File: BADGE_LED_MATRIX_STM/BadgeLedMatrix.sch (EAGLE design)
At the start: 106 parts, among them CN2 MICRO-USB-5P-340015001, IC1 STM32F0P, IC2 REG1117, Q1 12MHz, Q2 8MHz, U1 USBLC6SOT-23

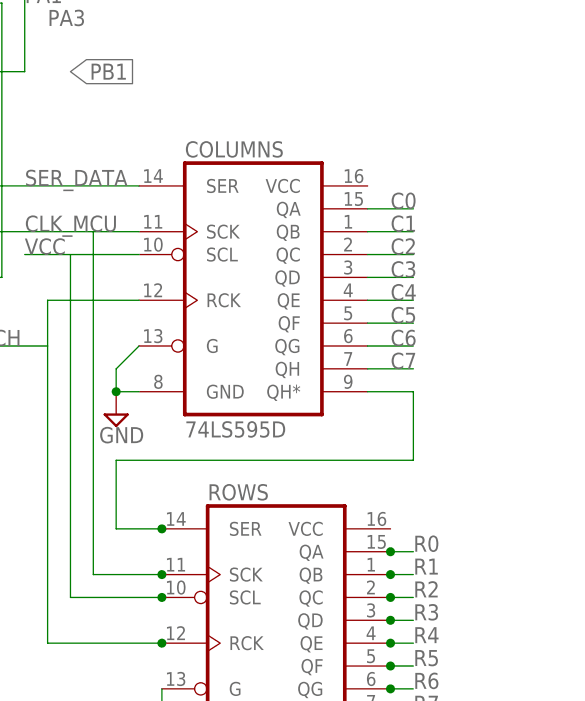
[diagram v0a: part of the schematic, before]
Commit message: Fix for connection of VCC from shift registers
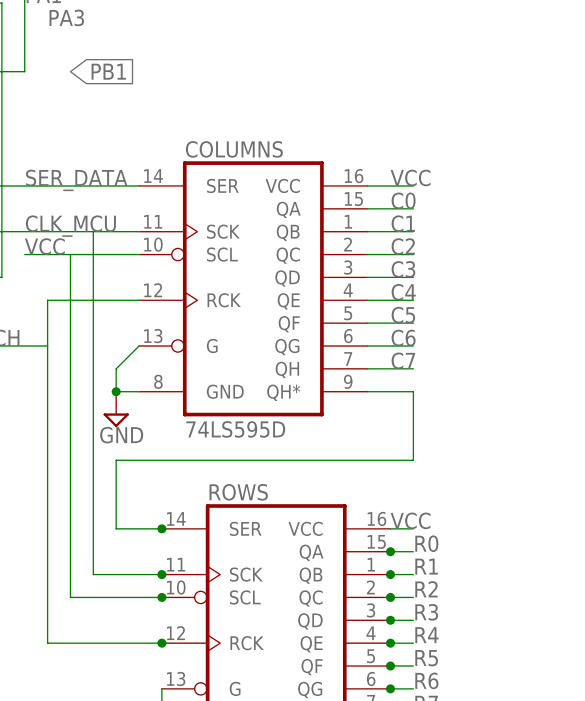
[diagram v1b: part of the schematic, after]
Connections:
- net VCC: now also COLUMNS.VCC, ROWS.VCC
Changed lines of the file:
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@@
 <label x="401.32" y="314.96" size="1.778" layer="95"/>
+</segment>
+<segment>
+<pinref part="COLUMNS" gate="A" pin="VCC"/>
+<wire x1="467.36" y1="289.56" x2="472.44" y2="289.56" width="0.1524" layer="91"/>
+<label x="469.9" y="289.56" size="1.778" layer="95"/>
+</segment>
+<segment>
+<pinref part="ROWS" gate="A" pin="VCC"/>
+<wire x1="469.9" y1="251.46" x2="472.44" y2="251.46" width="0.1524" layer="91"/>
+<label x="469.9" y="251.46" size="1.778" layer="95"/>
 </segment>
 </net>

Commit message: Small touch ups
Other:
- note added: "2"
- note added: "BSidesPR 2016 Led Matrix Badge"
- note added: "BSidesPR2016SCH"
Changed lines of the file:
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@@
 <wire x1="299.72" y1="243.84" x2="345.44" y2="243.84" width="0.1524" layer="94"/>
 <wire x1="345.44" y1="243.84" x2="345.44" y2="210.82" width="0.1524" layer="94"/>
+<text x="398.78" y="139.7" size="2.54" layer="94">BSidesPR 2016 Led Matrix Badge</text>
+<text x="411.48" y="129.54" size="2.54" layer="94">BSidesPR2016SCH</text>
+<text x="477.52" y="129.54" size="2.54" layer="94">2</text>
 </plain>
 <instances>
@@
 <instance part="PROTO1" gate="A" x="480.06" y="320.04"/>
 <instance part="FRAME1" gate="G$1" x="210.82" y="121.92"/>
-<instance part="FRAME1" gate="G$2" x="383.54" y="121.92"/>
+<instance part="FRAME1" gate="G$2" x="383.54" y="121.92" smashed="yes">
+<attribute name="LAST_DATE_TIME" x="396.24" y="123.19" size="2.54" layer="94"/>
+<attribute name="SHEET" x="469.9" y="123.19" size="2.54" layer="94"/>
+</instance>
 </instances>
 <busses>

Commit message: Added EPROM and wired up buttons
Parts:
- removed BTN1, BTN2, BTN3, BTN4: SWITCH-MOMENTARY-2SMD-REDUNDANT, SparkFun-Electromechanical:SWITCH-MOMENTARY-2SMD-REDUNDANT
- removed JP3: (no value), pinhead:PINHD-2X4
- removed JP4: (no value), pinhead:PINHD-2X2
- added DOWN, LEFT, RIGHT, UP: SWITCH-MOMENTARY-2SMD-REDUNDANT, SparkFun-Electromechanical:SWITCH-MOMENTARY-2SMD-REDUNDANT
- added U$6: AT93C66A, digital-ic:AT93C66A
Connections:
- removed net BTN1: BTN1.1, JP4.2
- removed net BTN2: BTN2.1, JP4.4
- removed net BTN3: BTN3.1, JP4.3
- removed net BTN4: BTN4.1, JP4.1
- net CLK_MCU: now also U$6.SK
- net GND: now also DOWN.2, LEFT.2, RIGHT.2, U$6.GND, UP.2; no longer BTN1.2, BTN2.2, BTN3.2, BTN4.2
- net PA0: now also UP.1; no longer JP3.3
- net PA1: now also LEFT.1; no longer JP3.6
- net PA2: now also RIGHT.1; no longer JP3.5
- net PA3: now also U$6.CS; no longer JP3.8
- net PA6: now also U$6.DO; no longer JP3.7
- net PB1: now also DOWN.1; no longer JP3.4
- net SER_DATA: now also U$6.DI
- net VCC: now also U$6.ORG, U$6.VCC; no longer JP3.1
- net VDDA: no longer JP3.2
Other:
- note added: "3"
- note added: "PROGRAM DEBUG ST-LINK"
- note added: "TOP BUTTONS"
- note removed: "2"
- moved on the sheet: JP2, PROTO, PROTO1, ST-LINK

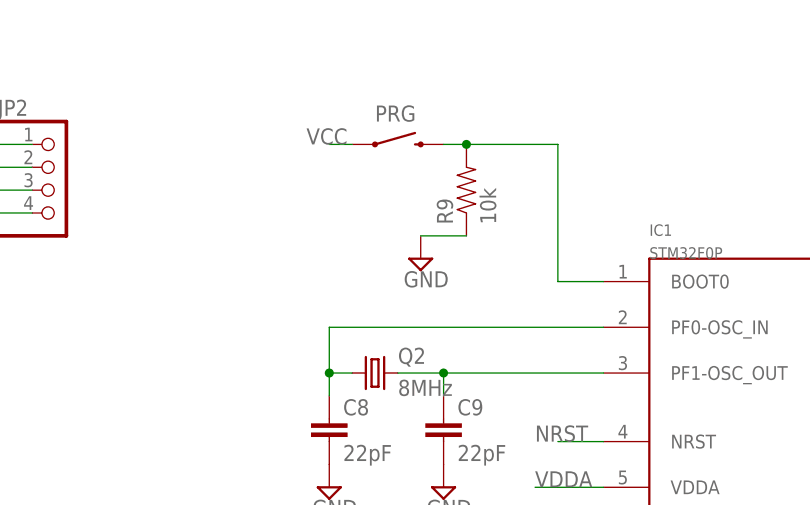
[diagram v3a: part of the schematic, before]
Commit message: Prototype 2, Ordered. Added EPROM, Slide Switch for PROG
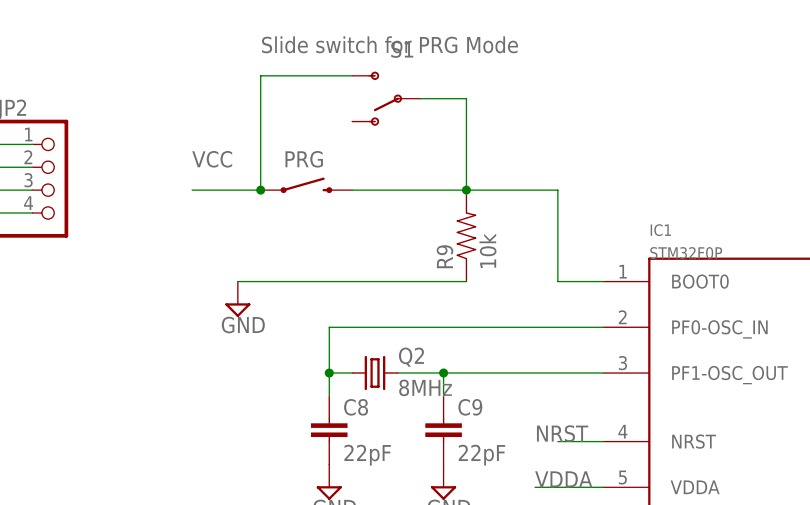
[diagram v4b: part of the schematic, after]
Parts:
- added S1: (no value), SparkFun-Electromechanical:SWITCH-SPDT-SMD-A
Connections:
- net N$4: now also S1.P
- net VCC: now also S1.S
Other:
- note added: "Slide switch for PRG Mode"
- moved on the sheet: PRG, R9
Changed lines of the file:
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@@
 <layer number="91" name="Nets" color="2" fill="1" visible="yes" active="yes"/>
 <layer number="92" name="Busses" color="1" fill="1" visible="yes" active="yes"/>
-<layer number="93" name="Pins" color="2" fill="1" visible="no" active="yes"/>
+<layer number="93" name="Pins" color="2" fill="1" visible="yes" active="yes"/>
 <layer number="94" name="Symbols" color="4" fill="1" visible="yes" active="yes"/>
 <layer number="95" name="Names" color="7" fill="1" visible="yes" active="yes"/>
@@
 <part name="U$6" library="digital-ic" deviceset="AT93C66A" device=""/>
 <part name="SUPPLY9" library="supply2" deviceset="GND" device=""/>
+<part name="S1" library="SparkFun-Electromechanical" deviceset="SWITCH-SPDT" device="-SMD-A"/>
 </parts>
 <sheets>
@@
 <text x="220.98" y="325.12" size="2.54" layer="95">TOP BUTTONS</text>
 <wire x1="248.92" y1="334.01" x2="248.92" y2="284.48" width="0.1524" layer="94"/>
+<text x="330.2" y="330.2" size="1.778" layer="96">Slide switch for PRG Mode</text>
 </plain>
 <instances>
@@
 </instance>
 <instance part="SUPPLY4" gate="GND" x="241.3" y="299.72"/>
-<instance part="R9" gate="G$1" x="353.06" y="314.96" rot="R90"/>
-<instance part="SUPPLY12" gate="GND" x="347.98" y="307.34"/>
-<instance part="PRG" gate="G$1" x="345.44" y="320.04" smashed="yes">
-<attribute name="NAME" x="342.9" y="322.58" size="1.778" layer="95"/>
+<instance part="R9" gate="G$1" x="353.06" y="309.88" rot="R90"/>
+<instance part="SUPPLY12" gate="GND" x="327.66" y="302.26"/>
+<instance part="PRG" gate="G$1" x="335.28" y="314.96" smashed="yes">
+<attribute name="NAME" x="332.74" y="317.5" size="1.778" layer="95"/>
 </instance>
 <instance part="RESET" gate="G$1" x="406.4" y="233.68" smashed="yes">
@@
 <instance part="U$6" gate="G$1" x="462.28" y="317.5"/>
 <instance part="SUPPLY9" gate="GND" x="474.98" y="304.8"/>
+<instance part="S1" gate="1" x="345.44" y="325.12" rot="R180"/>
 </instances>
 <busses>
@@
 <pinref part="R9" gate="G$1" pin="1"/>
 <pinref part="SUPPLY12" gate="GND" pin="GND"/>
-<wire x1="353.06" y1="309.88" x2="347.98" y2="309.88" width="0.1524" layer="91"/>
+<wire x1="353.06" y1="304.8" x2="327.66" y2="304.8" width="0.1524" layer="91"/>
 </segment>
 <segment>
@@
 <segment>
 <pinref part="PRG" gate="G$1" pin="1"/>
-<wire x1="340.36" y1="320.04" x2="337.82" y2="320.04" width="0.1524" layer="91"/>
-<label x="335.28" y="320.04" size="1.778" layer="95"/>
+<wire x1="330.2" y1="314.96" x2="322.58" y2="314.96" width="0.1524" layer="91"/>
+<label x="322.58" y="317.5" size="1.778" layer="95"/>
+<wire x1="330.2" y1="327.66" x2="330.2" y2="314.96" width="0.1524" layer="91"/>
+<junction x="330.2" y="314.96"/>
+<pinref part="S1" gate="1" pin="S"/>
+<wire x1="330.2" y1="327.66" x2="340.36" y2="327.66" width="0.1524" layer="91"/>
 </segment>
 <segment>
@@
 <segment>
 <pinref part="R9" gate="G$1" pin="2"/>
-<wire x1="350.52" y1="320.04" x2="353.06" y2="320.04" width="0.1524" layer="91"/>
+<wire x1="340.36" y1="314.96" x2="353.06" y2="314.96" width="0.1524" layer="91"/>
 <pinref part="IC1" gate="G$1" pin="BOOT0"/>
 <wire x1="368.3" y1="304.8" x2="363.22" y2="304.8" width="0.1524" layer="91"/>
-<wire x1="363.22" y1="304.8" x2="363.22" y2="320.04" width="0.1524" layer="91"/>
-<wire x1="363.22" y1="320.04" x2="353.06" y2="320.04" width="0.1524" layer="91"/>
-<junction x="353.06" y="320.04"/>
+<wire x1="363.22" y1="304.8" x2="363.22" y2="314.96" width="0.1524" layer="91"/>
+<wire x1="363.22" y1="314.96" x2="353.06" y2="314.96" width="0.1524" layer="91"/>
+<junction x="353.06" y="314.96"/>
 <pinref part="PRG" gate="G$1" pin="2"/>
-</segment>
-</net>
+<wire x1="353.06" y1="325.12" x2="353.06" y2="314.96" width="0.1524" layer="91"/>
+<pinref part="S1" gate="1" pin="P"/>
+<wire x1="347.98" y1="325.12" x2="353.06" y2="325.12" width="0.1524" layer="91"/>
+</segment>
+</net>
